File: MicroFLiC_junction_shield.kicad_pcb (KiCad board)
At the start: 2 copper layers, 98 x 53.3 mm, 81 parts, among them P1 14-way Micro-MaTch, P2 8-way Micro-MaTch, P3 6-way Micro-MaTch, P4 12-way Micro-MaTch, P5 1x4 Socket Strip R/A, P6 2x8 socket strip, Q1 TSM2314, Q2 TSM2314, Q3 TSM2314, Q4 TSM2314, SW1 Tactile Switch R/A, U1 23LCV1024, U2 PCA9306DP, U3 DS1338, X1 32.768kHz

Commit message: Changed part number or yellow LED
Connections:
- P4 pad 10: Net-(P4-Pad10) -> (no net)
- SHIELD1 pad 5V_6: Net-(SHIELD1-Pad5V_6) -> (no net)
- SHIELD1 pad NC: Net-(SHIELD1-PadNC) -> (no net)
- SHIELD1 pad RST2: Net-(SHIELD1-PadRST2) -> (no net)
- U1 pad 7: Net-(U1-Pad7) -> (no net)
- U3 pad 7: Net-(U3-Pad7) -> (no net)
- X1 pad 2: Net-(X1-Pad2) -> (no net)
- X1 pad 3: Net-(X1-Pad3) -> (no net)
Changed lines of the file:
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@@
     (zones 0)
     (modules 81)
-    (nets 103)
+    (nets 95)
   )
   (page A4)
@@
   (net 91 /MCUswitch/~MCU_OFF)
   (net 92 /MCUswitch/~SW_SENSE)
-  (net 93 "Net-(P4-Pad10)")
-  (net 94 /AD7)
-  (net 95 /MCUswitch/PWR_OFF)
-  (net 96 "Net-(SHIELD1-Pad5V_6)")
-  (net 97 "Net-(SHIELD1-PadRST2)")
-  (net 98 "Net-(SHIELD1-PadNC)")
-  (net 99 "Net-(U1-Pad7)")
-  (net 100 "Net-(U3-Pad7)")
-  (net 101 "Net-(X1-Pad2)")
-  (net 102 "Net-(X1-Pad3)")
+  (net 93 /AD7)
+  (net 94 /MCUswitch/PWR_OFF)
   (net_class Default "This is the default net class."
     (clearance 0.2)
@@
     (add_net "Net-(C6-Pad1)")
     (add_net "Net-(D1-Pad1)")
-    (add_net "Net-(P4-Pad10)")
     (add_net "Net-(Q1-Pad3)")
     (add_net "Net-(Q2-Pad3)")
     (add_net "Net-(Q3-Pad3)")
-    (add_net "Net-(SHIELD1-Pad5V_6)")
-    (add_net "Net-(SHIELD1-PadNC)")
-    (add_net "Net-(SHIELD1-PadRST2)")
-    (add_net "Net-(U1-Pad7)")
-    (add_net "Net-(U3-Pad7)")
-    (add_net "Net-(X1-Pad2)")
-    (add_net "Net-(X1-Pad3)")
   )
   (module Capacitors_SMD:C_0805 (layer F.Cu)
@@
     (pad 9 smd rect (at 3.175 -2.54 90) (size 1.5 3.5) (layers F.Cu F.Paste F.Mask)
       (net 31 /SH_~LDAC))
-    (pad 10 smd rect (at 4.445 2.5 90) (size 1.5 3.5) (layers F.Cu F.Paste F.Mask)
-      (net 93 "Net-(P4-Pad10)"))
+    (pad 10 smd rect (at 4.445 2.5 90) (size 1.5 3.5) (layers F.Cu F.Paste F.Mask))
     (pad 11 smd rect (at 5.715 -2.54 90) (size 1.5 3.5) (layers F.Cu F.Paste F.Mask)
       (net 32 /SCL1))
@@
     (pad 6 smd rect (at 2.7 0.635) (size 1.55 0.6) (layers F.Cu F.Paste F.Mask)
       (net 85 /SPCK))
-    (pad 7 smd rect (at 2.7 -0.635) (size 1.55 0.6) (layers F.Cu F.Paste F.Mask)
-      (net 99 "Net-(U1-Pad7)"))
+    (pad 7 smd rect (at 2.7 -0.635) (size 1.55 0.6) (layers F.Cu F.Paste F.Mask))
     (pad 8 smd rect (at 2.7 -1.905) (size 1.55 0.6) (layers F.Cu F.Paste F.Mask)
       (net 1 +3V3))
@@
     (pad 6 smd rect (at 2.7 0.635) (size 1.55 0.6) (layers F.Cu F.Paste F.Mask)
       (net 37 /LCDandRTC/SCL_5V))
-    (pad 7 smd rect (at 2.7 -0.635) (size 1.55 0.6) (layers F.Cu F.Paste F.Mask)
-      (net 100 "Net-(U3-Pad7)"))
+    (pad 7 smd rect (at 2.7 -0.635) (size 1.55 0.6) (layers F.Cu F.Paste F.Mask))
     (pad 8 smd rect (at 2.7 -1.905) (size 1.55 0.6) (layers F.Cu F.Paste F.Mask)
       (net 3 +5V))
@@
     (pad 1 smd rect (at -2.75 1.6 180) (size 1.3 1.9) (layers F.Cu F.Paste F.Mask)
       (net 88 /LCDandRTC/X1))
-    (pad 2 smd rect (at 2.75 1.6 180) (size 1.3 1.9) (layers F.Cu F.Paste F.Mask)
-      (net 101 "Net-(X1-Pad2)"))
-    (pad 3 smd rect (at 2.75 -1.6 180) (size 1.3 1.9) (layers F.Cu F.Paste F.Mask)
-      (net 102 "Net-(X1-Pad3)"))
+    (pad 2 smd rect (at 2.75 1.6 180) (size 1.3 1.9) (layers F.Cu F.Paste F.Mask))
+    (pad 3 smd rect (at 2.75 -1.6 180) (size 1.3 1.9) (layers F.Cu F.Paste F.Mask))
     (pad 4 smd rect (at -2.75 -1.6 180) (size 1.3 1.9) (layers F.Cu F.Paste F.Mask)
       (net 89 /LCDandRTC/X2))
@@
       (net 29 /SH1))
     (pad AD7 thru_hole oval (at 68.58 -2.54 90) (size 2.54 1.524) (drill 1.016) (layers *.Cu *.Mask F.SilkS)
-      (net 94 /AD7))
+      (net 93 /AD7))
     (pad AD6 thru_hole oval (at 66.04 -2.54 90) (size 2.54 1.524) (drill 1.016) (layers *.Cu *.Mask F.SilkS)
       (net 11 /SW4))
@@
       (net 82 /LCDandRTC/~LCD_CS))
     (pad 42 thru_hole circle (at 93.98 -22.86) (size 1.524 1.524) (drill 1.016) (layers *.Cu *.Mask F.SilkS)
-      (net 95 /MCUswitch/PWR_OFF))
+      (net 94 /MCUswitch/PWR_OFF))
     (pad 43 thru_hole circle (at 96.52 -22.86) (size 1.524 1.524) (drill 1.016) (layers *.Cu *.Mask F.SilkS)
       (net 92 /MCUswitch/~SW_SENSE))
@@
     (pad MISO thru_hole circle (at 63.627 -30.48 90) (size 1.524 1.524) (drill 1.016) (layers *.Cu *.Mask F.SilkS)
       (net 6 /MISO))
-    (pad 5V_6 thru_hole circle (at 66.167 -30.48 90) (size 1.524 1.524) (drill 1.016) (layers *.Cu *.Mask F.SilkS)
-      (net 96 "Net-(SHIELD1-Pad5V_6)"))
+    (pad 5V_6 thru_hole circle (at 66.167 -30.48 90) (size 1.524 1.524) (drill 1.016) (layers *.Cu *.Mask F.SilkS))
     (pad SPCK thru_hole circle (at 63.627 -27.94 90) (size 1.524 1.524) (drill 1.016) (layers *.Cu *.Mask F.SilkS)
       (net 85 /SPCK))
-    (pad RST2 thru_hole circle (at 63.627 -25.4 90) (size 1.524 1.524) (drill 1.016) (layers *.Cu *.Mask F.SilkS)
-      (net 97 "Net-(SHIELD1-PadRST2)"))
+    (pad RST2 thru_hole circle (at 63.627 -25.4 90) (size 1.524 1.524) (drill 1.016) (layers *.Cu *.Mask F.SilkS))
     (pad MOSI thru_hole circle (at 66.167 -27.94 90) (size 1.524 1.524) (drill 1.016) (layers *.Cu *.Mask F.SilkS)
       (net 8 /MOSI))
@@
     (pad IOR thru_hole oval (at 30.48 -2.54 90) (size 2.54 1.524) (drill 1.016) (layers *.Cu *.Mask F.SilkS)
       (net 20 /IOREF))
-    (pad NC thru_hole oval (at 27.94 -2.54 90) (size 2.54 1.524) (drill 1.016) (layers *.Cu *.Mask F.SilkS)
-      (net 98 "Net-(SHIELD1-PadNC)"))
+    (pad NC thru_hole oval (at 27.94 -2.54 90) (size 2.54 1.524) (drill 1.016) (layers *.Cu *.Mask F.SilkS))
     (model jakub.3dshapes/Arduino/ArduinoDUE/ArduinoDUE.wrl
       (at (xyz -0.09 0 -0.5748))
@@
     )
     (pad 1 thru_hole rect (at 0 0) (size 1.524 1.524) (drill 1.016) (layers *.Cu *.Mask F.SilkS)
-      (net 94 /AD7))
+      (net 93 /AD7))
   )
   (module TO_SOT_Packages_SMD:SOT-23 (layer F.Cu)
@@
     (fp_line (start 1.49982 -0.65024) (end 1.49982 0.0508) (layer F.SilkS) (width 0.15))
     (pad 1 smd rect (at -0.95 1.00076 270) (size 0.8001 0.8001) (layers F.Cu F.Paste F.Mask)
-      (net 95 /MCUswitch/PWR_OFF))
+      (net 94 /MCUswitch/PWR_OFF))
     (pad 2 smd rect (at 0.95 1.00076 270) (size 0.8001 0.8001) (layers F.Cu F.Paste F.Mask)
       (net 2 GND))
@@
     (fp_line (start -0.6 -0.875) (end 0.6 -0.875) (layer F.SilkS) (width 0.15))
     (pad 1 smd rect (at -0.95 0 270) (size 0.7 1.3) (layers F.Cu F.Paste F.Mask)
-      (net 95 /MCUswitch/PWR_OFF))
+      (net 94 /MCUswitch/PWR_OFF))
     (pad 2 smd rect (at 0.95 0 270) (size 0.7 1.3) (layers F.Cu F.Paste F.Mask)
       (net 2 GND))
@@
   (segment (start 199.07 109.474) (end 200.953 109.474) (width 0.508) (layer F.Cu) (net 92))
   (segment (start 200.953 109.474) (end 202.477 110.998) (width 0.508) (layer F.Cu) (net 92))
-  (segment (start 192.532 126.492) (end 192.532 129.54) (width 0.508) (layer F.Cu) (net 94))
-  (segment (start 217.932 109.22) (end 216.916 109.22) (width 0.508) (layer B.Cu) (net 95))
-  (segment (start 215.9 110.236) (end 199.39 110.236) (width 0.508) (layer B.Cu) (net 95))
-  (segment (start 216.916 109.22) (end 215.9 110.236) (width 0.508) (layer B.Cu) (net 95))
-  (segment (start 198.374 111.252) (end 199.39 110.236) (width 0.508) (layer B.Cu) (net 95))
-  (segment (start 197.69324 111.252) (end 197.11924 111.826) (width 0.508) (layer F.Cu) (net 95))
-  (via (at 198.374 111.252) (size 1) (drill 0.5) (layers F.Cu B.Cu) (net 95))
-  (segment (start 197.69324 111.252) (end 198.374 111.252) (width 0.508) (layer F.Cu) (net 95))
-  (segment (start 195.326 111.826) (end 197.11924 111.826) (width 0.508) (layer F.Cu) (net 95))
+  (segment (start 192.532 126.492) (end 192.532 129.54) (width 0.508) (layer F.Cu) (net 93))
+  (segment (start 217.932 109.22) (end 216.916 109.22) (width 0.508) (layer B.Cu) (net 94))
+  (segment (start 215.9 110.236) (end 199.39 110.236) (width 0.508) (layer B.Cu) (net 94))
+  (segment (start 216.916 109.22) (end 215.9 110.236) (width 0.508) (layer B.Cu) (net 94))
+  (segment (start 198.374 111.252) (end 199.39 110.236) (width 0.508) (layer B.Cu) (net 94))
+  (segment (start 197.69324 111.252) (end 197.11924 111.826) (width 0.508) (layer F.Cu) (net 94))
+  (via (at 198.374 111.252) (size 1) (drill 0.5) (layers F.Cu B.Cu) (net 94))
+  (segment (start 197.69324 111.252) (end 198.374 111.252) (width 0.508) (layer F.Cu) (net 94))
+  (segment (start 195.326 111.826) (end 197.11924 111.826) (width 0.508) (layer F.Cu) (net 94))
   (zone (net 2) (net_name GND) (layer F.Cu) (hatch edge 0.508)
     (connect_pads (clearance 0.508))

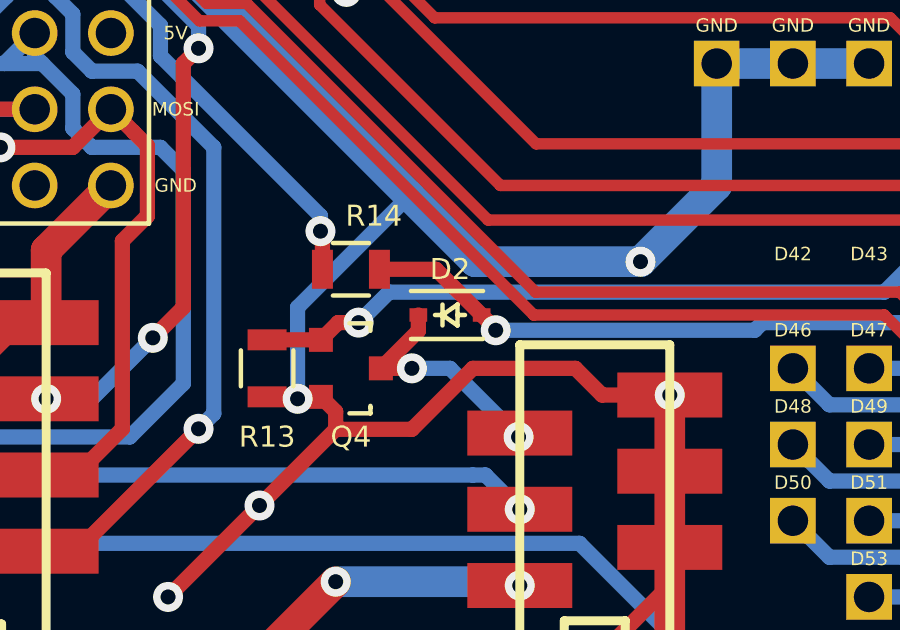
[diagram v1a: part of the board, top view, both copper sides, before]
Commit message: Changed SHIELD1 to A1, changed SOD-323 footprint for easier soldering
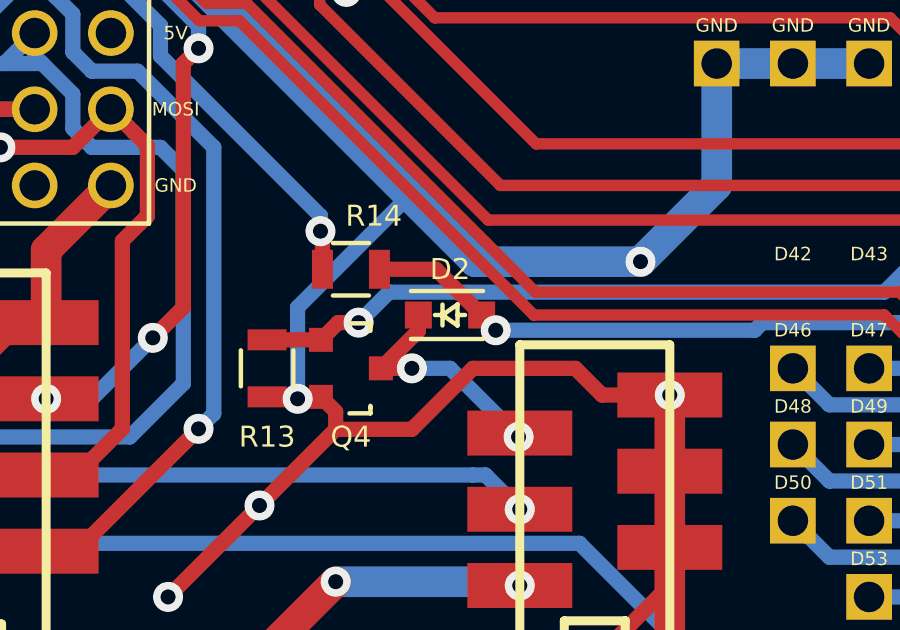
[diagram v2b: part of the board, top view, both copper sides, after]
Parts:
- A1: renamed from SHIELD1; value ARDUINO_DUE_SHIELD -> Arduino DUE
- D2: footprint Diodes_SMD:SOD-323 -> jakub:SOD-323
- P5: value 1x4 Socket Strip R/A -> 1x4 socket strip R/A
- SP1: value PIEZO SOUNDER -> Piezo sounder
- SW1: value Tactile Switch R/A -> Tactile switch R/A
- U2: value PCA9306DP -> PCA9306

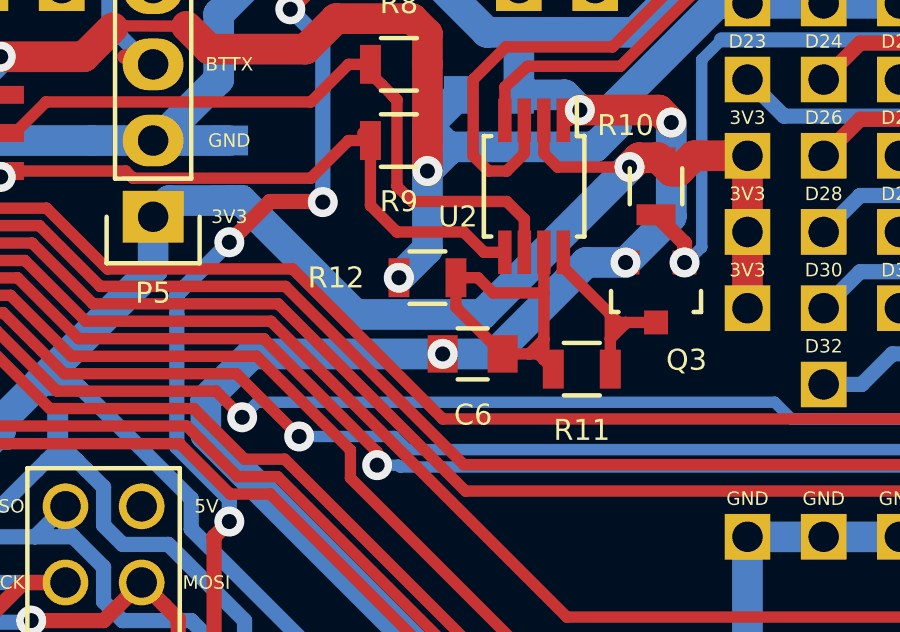
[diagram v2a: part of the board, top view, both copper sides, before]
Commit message: Changed layout of I2C buffer enabling
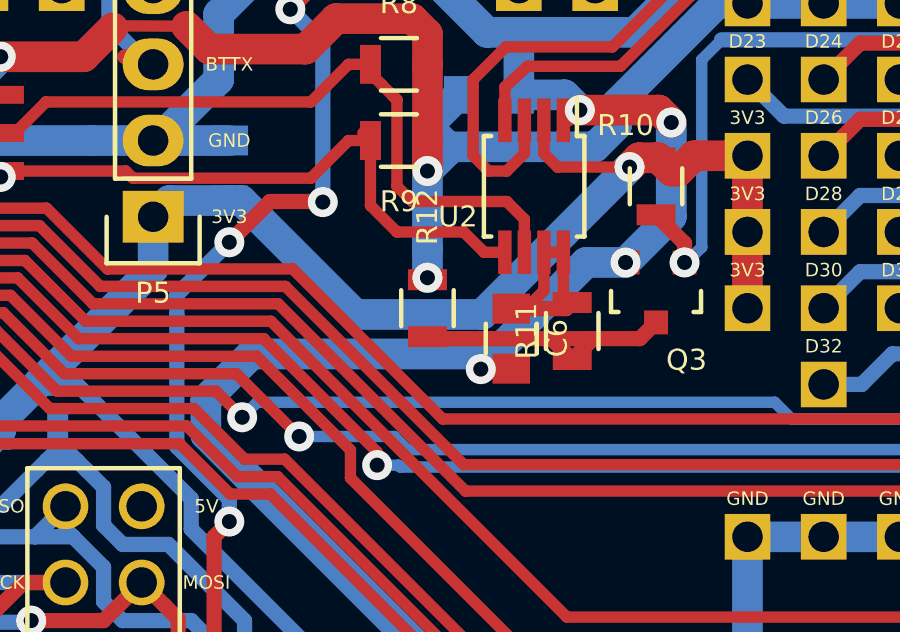
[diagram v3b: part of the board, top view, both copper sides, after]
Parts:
- C6: value 100n -> 100p
- R12: value 1k5 -> 100k
- moved C6 1.38 mm to (202.4, 96.0), turned to 270 degrees
- moved R11 1.31 mm to (204.5, 95.8), turned to 90 degrees
- moved R12 1.02 mm to (199.6, 95.0), turned to 90 degrees
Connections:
- R11 pad 1: Net-(C6-Pad1) -> Net-(Q3-Pad3)
- R11 pad 2: Net-(Q3-Pad3) -> Net-(C6-Pad1)
- R12 pad 1: Net-(C6-Pad1) -> Net-(Q3-Pad3)
- U2 pad 8: Net-(Q3-Pad3) -> Net-(C6-Pad1)
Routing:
- net Net-(C6-Pad1): track 12.5 -> 7.68 mm
- net Net-(Q3-Pad3): track 6.43 -> 9.84 mm
- net GND: track 400.1 -> 401.7 mm

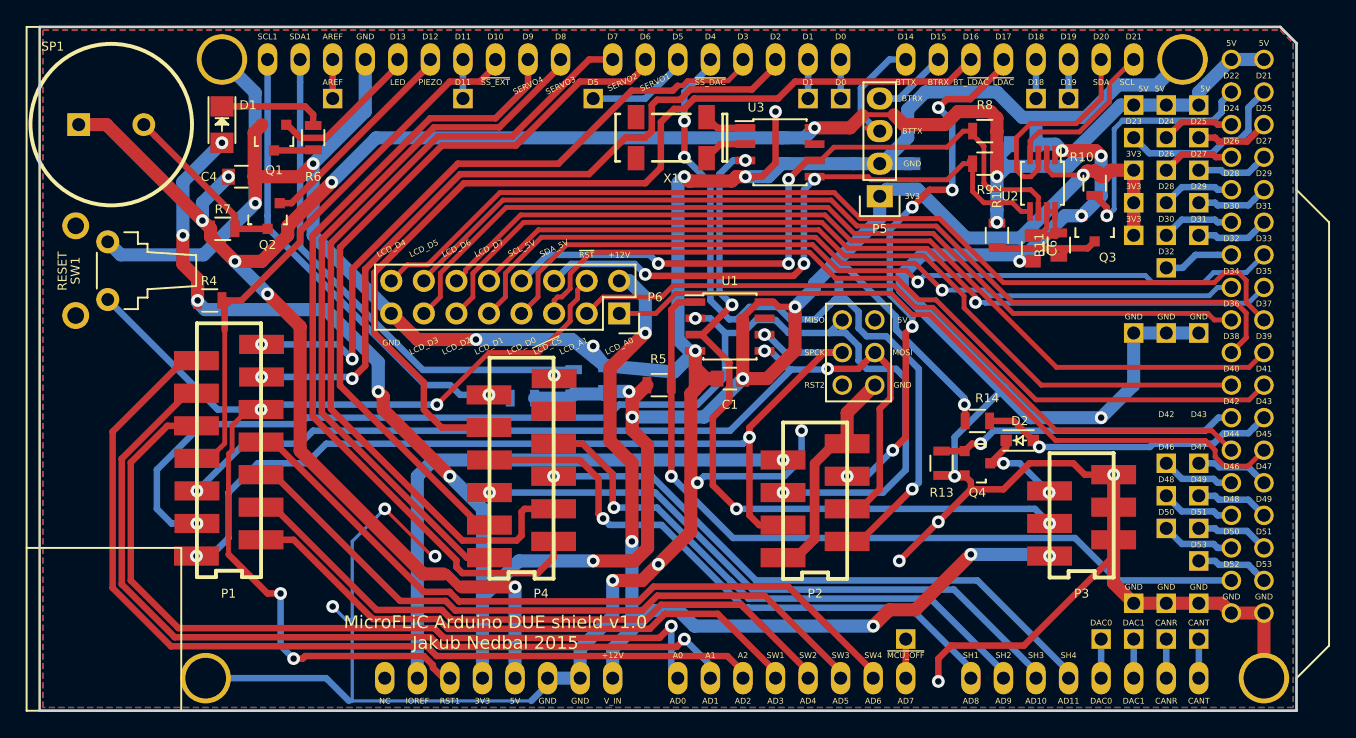
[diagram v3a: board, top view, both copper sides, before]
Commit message: Changed LCD shield from Wire to Wire1
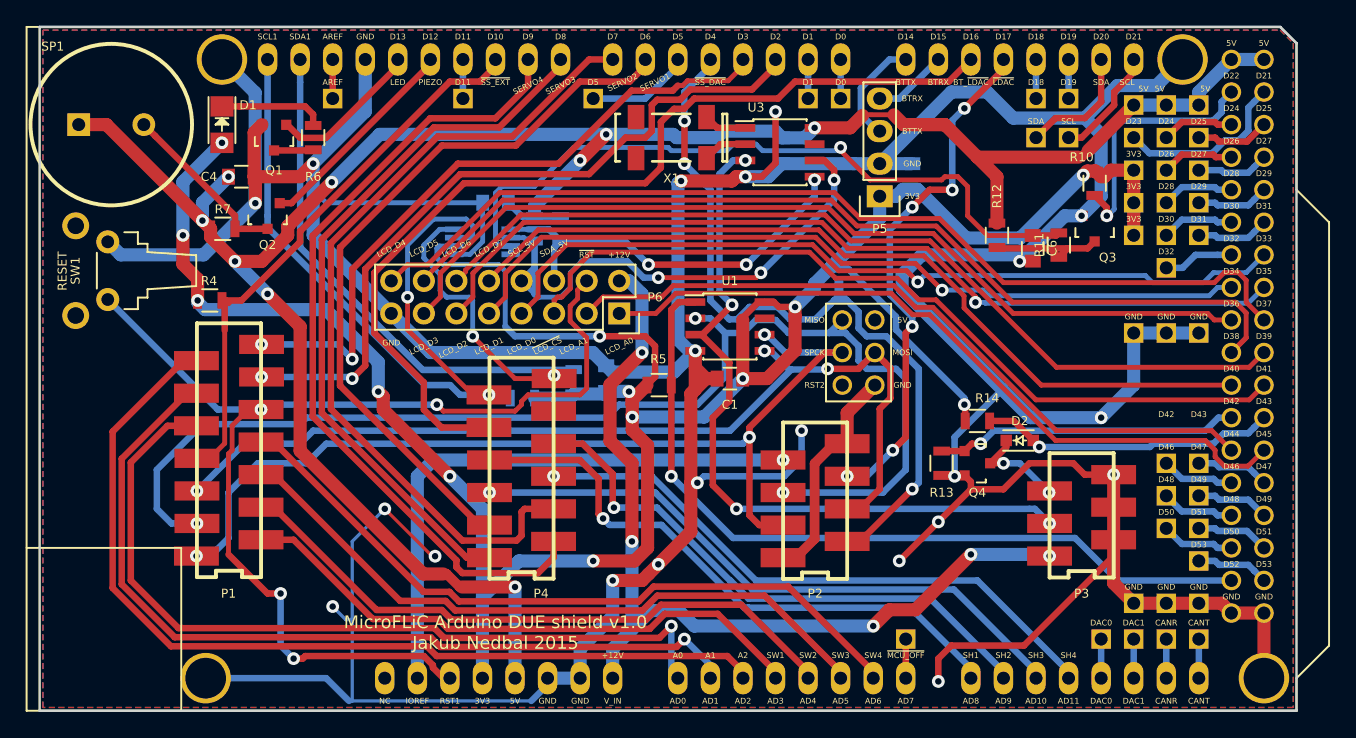
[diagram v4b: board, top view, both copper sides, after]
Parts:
- added PP20: CONN_01X01, jakub:PIN_ARRAY_1, F.Cu at (202.7, 87.4)
- added PP21: CONN_01X01, jakub:PIN_ARRAY_1, F.Cu at (205.2, 87.4)
- R8, R9, U2: moved to B.Cu
- moved U2 43.9 mm to (159.5, 95.5), turned to 0 degrees
- moved C5 41.4 mm to (160.5, 92.5), turned to 180 degrees
- moved R8 35.9 mm to (163.6, 94.5), turned to 90 degrees
- moved R9 33.5 mm to (165.6, 94.5), turned to 90 degrees
- renumbered PP20 to PP22, PP21 to PP23, PP22 to PP24, PP23 to PP25, PP24 to PP26, PP25 to PP27, PP26 to PP28, PP27 to PP29, PP28 to PP30, PP29 to PP31, PP30 to PP32, PP31 to PP33, PP32 to PP34, PP33 to PP35, PP34 to PP36, PP35 to PP37, PP36 to PP38, PP37 to PP39, PP38 to PP40, PP39 to PP41, PP40 to PP42, PP41 to PP43
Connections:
- net Net-(C6-Pad1) renamed /LCDandRTC/I2C_EN
- A1 pad 20: /LCDandRTC/SDA -> /SDA
- A1 pad 21: /LCDandRTC/SCL -> /SCL
- A1 pad SCL1: /SCL1 -> /LCDandRTC/SCL1
- A1 pad SDA1: /SDA1 -> /LCDandRTC/SDA1
- P4 pad 11: /SCL1 -> /LCDandRTC/SCL1
- P4 pad 12: /SDA1 -> /LCDandRTC/SDA1
- R1 pad 2: /SCL1 -> /LCDandRTC/SCL1
- R2 pad 2: /SDA1 -> /LCDandRTC/SDA1
- U2 pad 3: /LCDandRTC/SDA -> /LCDandRTC/SCL1
- U2 pad 4: /LCDandRTC/SCL -> /LCDandRTC/SDA1
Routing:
- net /LCDandRTC/SCL1: track 0.00 -> 61.0 mm, vias 0 -> 2
- net /LCDandRTC/SDA1: track 0.00 -> 61.0 mm, vias 0 -> 2
- net /LCDandRTC/I2C_EN: track 7.68 -> 56.9 mm, vias 0 -> 1
- net /SDA1: track 40.6 -> 0.00 mm, vias 1 -> 0
- net /SCL1: track 37.6 -> 0.00 mm, vias 1 -> 0
- net +3V3: track 186.8 -> 210.5 mm, vias 12 -> 13
- net /LCDandRTC/SDA: track 16.7 -> 0.00 mm
- net /LCDandRTC/SDA_5V: track 48.4 -> 32.1 mm
- net /LCDandRTC/SCL_5V: track 55.5 -> 41.8 mm
- net /LCDandRTC/SCL: track 12.6 -> 0.00 mm
- net GND: track 401.7 -> 413.6 mm, vias 25 -> 21
- net +5V: track 169.7 -> 180.4 mm
- net /SDA: track 0.00 -> 9.54 mm
- net /SCL: track 0.00 -> 8.80 mm
- net /LCDandRTC/~RST: track 83.5 -> 89.0 mm
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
